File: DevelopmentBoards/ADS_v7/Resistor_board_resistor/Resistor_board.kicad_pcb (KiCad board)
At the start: 2 copper layers, 39 x 12.8 mm, 6 parts, among them J1 Conn_01x06_Pin, SW1 SW_SPDT_312

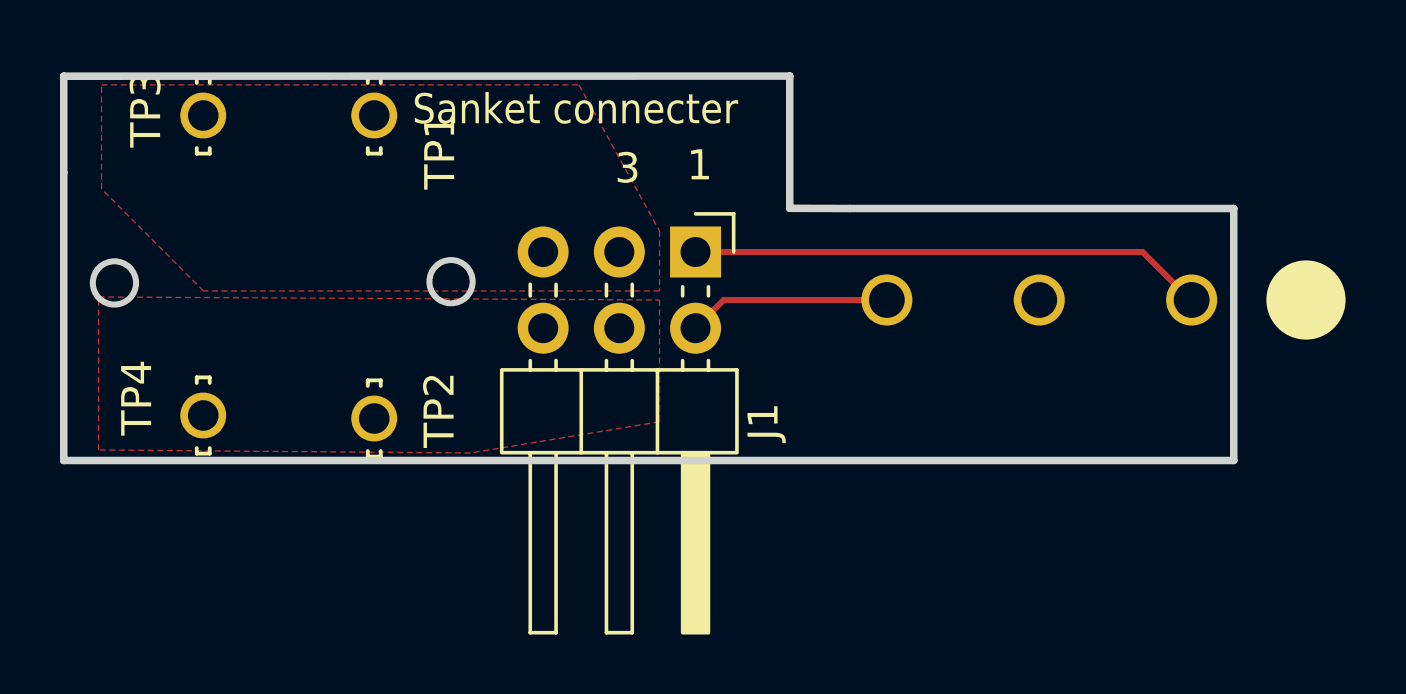
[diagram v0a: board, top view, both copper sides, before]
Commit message: Corrected board settings for resistor and nichrome boards also. Replaced pour to thick copper trace on resistor and nichrome boards
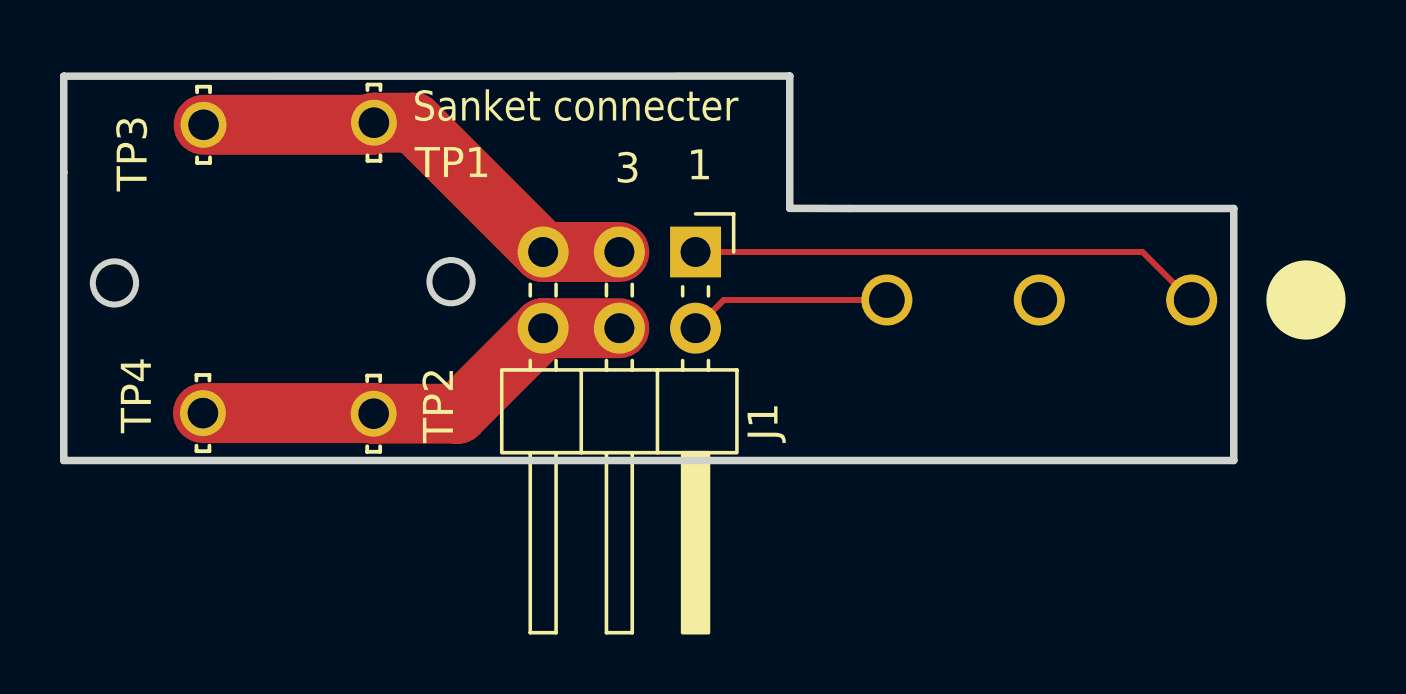
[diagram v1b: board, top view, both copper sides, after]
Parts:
- moved TP3 0.31 mm to (114.6, 53.1)
- moved TP1 0.24 mm to (120.3, 53.0)
- moved TP2 0.16 mm to (120.3, 62.7)
- moved TP4 0.08 mm to (114.6, 62.7)
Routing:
- net /BurnWireIN: track 0.00 -> 15.7 mm
- net /GND: track 0.00 -> 15.1 mm
- removed copper zone on F.Cu, net /BurnWireIN
- removed copper zone on F.Cu, net /GND
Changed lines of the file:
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@@
 	(footprint "5021:TP_5021"
 		(layer "F.Cu")
-		(at 114.59 52.75 -90)
+		(at 114.6 53.06 -90)
 		(property "Reference" "TP3"
-			(at -0.2 1.9 90)
+			(at 0.95 2.36 270)
 			(layer "F.SilkS")
 			(effects
@@
 		)
 		(property "Value" "5021"
-			(at 2.925 2.65 90)
-			(layer "F.Fab")
+			(at 3.99 2.55 90)
+			(layer "F.Fab")
+			(hide yes)
 			(effects
 				(font
@@
 	(footprint "5021:TP_5021"
 		(layer "F.Cu")
-		(at 114.59 62.75 -90)
+		(at 114.58 62.67 -90)
 		(property "Reference" "TP4"
 			(at -0.6 2.2 90)
@@
 	(footprint "5021:TP_5021"
 		(layer "F.Cu")
-		(at 120.29 52.75 -90)
+		(at 120.28 52.99 -90)
 		(property "Reference" "TP1"
-			(at 1.2 -2.2 90)
+			(at 1.35 -2.63 180)
 			(layer "F.SilkS")
 			(effects
@@
 	(footprint "5021:TP_5021"
 		(layer "F.Cu")
-		(at 120.29 62.85 -90)
+		(at 120.27 62.69 -90)
 		(property "Reference" "TP2"
 			(at -0.29 -2.18 90)
@@
 		)
 		(property "Value" "SW_SPDT_312"
-			(at 5.08 0 0)
+			(at 4.9074 -2.17 0)
 			(unlocked yes)
 			(layer "B.Fab")
@@
 	)
 	(gr_text "Sanket connecter"
-		(at 121.56 53.13 0)
+		(at 121.57 53.04 0)
 		(layer "F.SilkS")
 		(effects
@@
 			(justify left bottom mirror)
 		)
+	)
+	(segment
+		(start 120.21 53.06)
+		(end 120.28 52.99)
+		(width 2)
+		(layer "F.Cu")
+		(net "/BurnWireIN")
+	)
+	(segment
+		(start 121.61 52.99)
+		(end 120.28 52.99)
+		(width 2)
+		(layer "F.Cu")
+		(net "/BurnWireIN")
+	)
+	(segment
+		(start 128.46 57.3)
+		(end 125.92 57.3)
+		(width 2)
+		(layer "F.Cu")
+		(net "/BurnWireIN")
+	)
+	(segment
+		(start 125.92 57.3)
+		(end 121.61 52.99)
+		(width 2)
+		(layer "F.Cu")
+		(net "/BurnWireIN")
+	)
+	(segment
+		(start 114.6 53.06)
+		(end 120.21 53.06)
+		(width 2)
+		(layer "F.Cu")
+		(net "/BurnWireIN")
+	)
+	(segment
+		(start 120.25 62.67)
+		(end 120.27 62.69)
+		(width 2)
+		(layer "F.Cu")
+		(net "/GND")
+	)
+	(segment
+		(start 123.07 62.69)
+		(end 125.92 59.84)
+		(width 2)
+		(layer "F.Cu")
+		(net "/GND")
+	)
+	(segment
+		(start 114.58 62.67)
+		(end 120.25 62.67)
+		(width 2)
+		(layer "F.Cu")
+		(net "/GND")
+	)
+	(segment
+		(start 125.92 59.84)
+		(end 128.46 59.84)
+		(width 2)
+		(layer "F.Cu")
+		(net "/GND")
+	)
+	(segment
+		(start 120.27 62.69)
+		(end 123.07 62.69)
+		(width 2)
+		(layer "F.Cu")
+		(net "/GND")
 	)
 	(segment
@@
 	)
 	(zone
-		(net "/BurnWireIN")
-		(layer "F.Cu")
-		(hatch full 0.5)
-		(connect_pads
-			(clearance 0.5)
-		)
-		(min_thickness 0.25)
-		(fill yes
-			(thermal_gap 0.5)
-			(thermal_bridge_width 0.5)
-			(island_removal_mode 0)
-		)
-		(polygon
-			(pts
-				(xy 111.2 51.73) (xy 127.113103 51.73) (xy 129.8 56.6) (xy 129.8 58.6) (xy 114.6 58.6) (xy 111.2 55.2)
-			)
-		)
-	)
-	(zone
-		(net "/GND")
-		(layer "F.Cu")
-		(hatch full 0.5)
-		(priority 1)
-		(connect_pads
-			(clearance 0.5)
-		)
-		(min_thickness 0.25)
-		(fill yes
-			(thermal_gap 0.5)
-			(thermal_bridge_width 0.5)
-			(island_removal_mode 0)
-		)
-		(polygon
-			(pts
-				(xy 111.1 58.8) (xy 129.8 58.9) (xy 129.8 62.96) (xy 123.5 64) (xy 111.1 63.9)
-			)
-		)
-	)
-	(zone
 		(net "/DeployerDetectionSWOUT")
-		(layer "F.Cu")
-		(hatch none 0.1)
-		(priority 30002)
-		(attr
-			(teardrop
-				(type padvia)
-			)
-		)
-		(connect_pads yes
-			(clearance 0)
-		)
-		(min_thickness 0.0254)
-		(fill yes
-			(island_removal_mode 1)
-		)
-		(polygon
-			(pts
-				(xy 146.388954 57.647533) (xy 146.247533 57.788954) (xy 146.723139 59.147003) (xy 147.522304 58.922304)
-				(xy 147.784403 58.085739)
-			)
-		)
-	)
-	(zone
-		(net "/DeployerDetectionSWIN")
 		(layer "F.Cu")
 		(hatch none 0.1)
@@
 		(attr
 			(teardrop
+				(type padvia)
+			)
+		)
+		(connect_pads yes
+			(clearance 0)
+		)
+		(min_thickness 0.0254)
+		(fill yes
+			(island_removal_mode 1)
+		)
+		(polygon
+			(pts
+				(xy 146.388954 57.647533) (xy 146.247533 57.788954) (xy 146.723139 59.147003) (xy 147.522304 58.922304)
+				(xy 147.784403 58.085739)
+			)
+		)
+	)
+	(zone
+		(net "/DeployerDetectionSWIN")
+		(layer "F.Cu")
+		(hatch none 0.1)
+		(priority 30000)
+		(attr
+			(teardrop

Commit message: ADS v7: Corrected layout of converter, replaced tp pads with thp pads in resistor board, some other minor trace layout changes
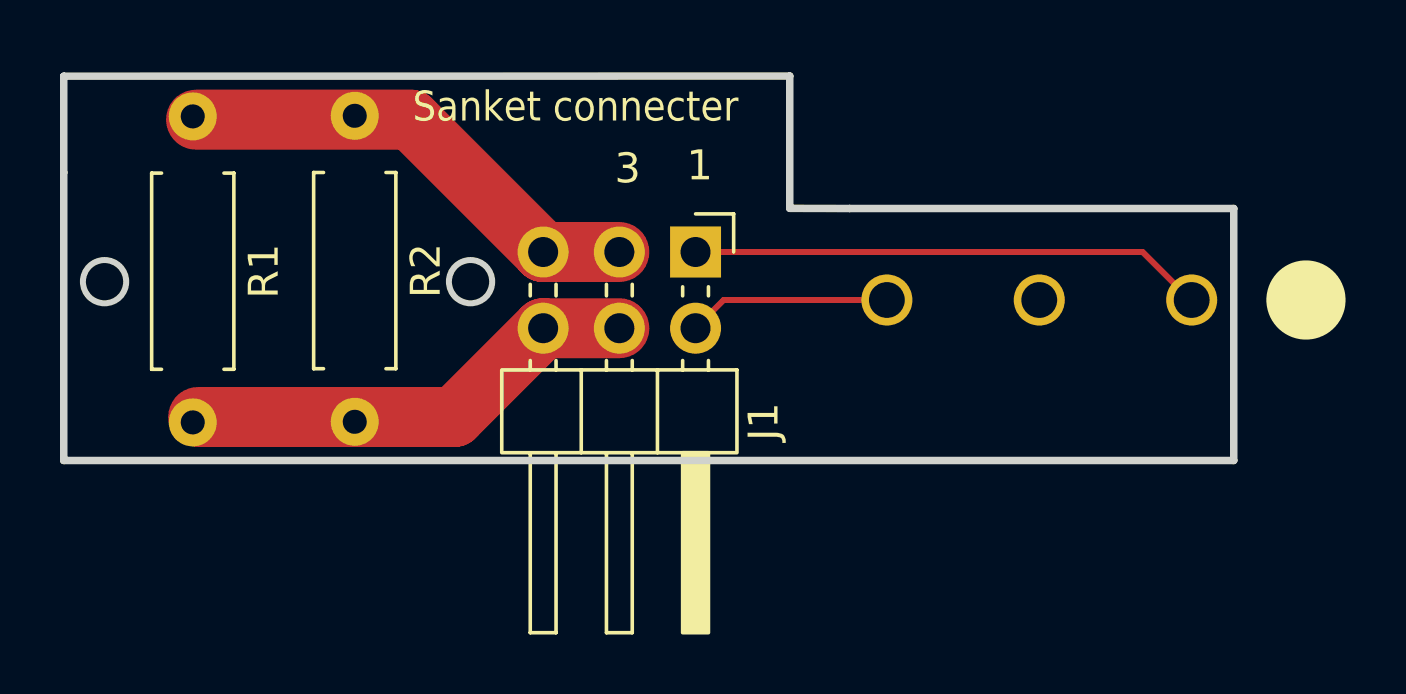
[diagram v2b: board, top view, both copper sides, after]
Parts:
- removed TP1, TP2, TP3, TP4: 5021, 5021:TP_5021
- added R1: R, Resistor_THT:R_Axial_DIN0207_L6.3mm_D2.5mm_P7.62mm_Horizontal, F.Cu at (114.2, 54.1)
- added R2: R, Resistor_THT:R_Axial_DIN0207_L6.3mm_D2.5mm_P7.62mm_Horizontal, F.Cu at (119.6, 54.1)
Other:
- outline, holes or cut-outs redrawn
